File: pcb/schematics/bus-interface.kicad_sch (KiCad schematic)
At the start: 28 parts, among them U3 LCMXO2-1200HC-4TG100I

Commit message: add shield
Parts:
- U: renamed from C31; value 1u -> (none); footprint Capacitor_SMD:C_0805_2012Metric -> (none)
- U: renamed from C24; value 10n -> (none); footprint Capacitor_SMD:C_0402_1005Metric -> (none)
- U: renamed from C22; value 100n -> (none); footprint Capacitor_SMD:C_0603_1608Metric -> (none)
- U: renamed from U3; value LCMXO2-1200HC-4TG100I -> (none); footprint LCMXO2-1200HC-4TG100I:Lattice_Semiconductor-LCMXO2-1200HC-4TG100I-Level_C -> (none)
- U: renamed from C21; value 100n -> (none); footprint Capacitor_SMD:C_0603_1608Metric -> (none)
- U: renamed from C8; value 10n -> (none); footprint Capacitor_SMD:C_0402_1005Metric -> (none)
- U: renamed from C9; value 10n -> (none); footprint Capacitor_SMD:C_0402_1005Metric -> (none)
- U: renamed from C28; value 10n -> (none); footprint Capacitor_SMD:C_0402_1005Metric -> (none)
- U: renamed from C29; value 100n -> (none); footprint Capacitor_SMD:C_0603_1608Metric -> (none)
- U: renamed from C30; value 100n -> (none); footprint Capacitor_SMD:C_0603_1608Metric -> (none)
- U: renamed from C5; value 1u -> (none); footprint Capacitor_SMD:C_0805_2012Metric -> (none)
- U: renamed from C10; value 10n -> (none); footprint Capacitor_SMD:C_0402_1005Metric -> (none)
- U: renamed from C26; value 10n -> (none); footprint Capacitor_SMD:C_0402_1005Metric -> (none)
- U: renamed from C18; value 100n -> (none); footprint Capacitor_SMD:C_0603_1608Metric -> (none)
- U: renamed from C6; value 100n -> (none); footprint Capacitor_SMD:C_0603_1608Metric -> (none)
- U: renamed from C25; value 10n -> (none); footprint Capacitor_SMD:C_0402_1005Metric -> (none)
- U: renamed from C20; value 1u -> (none); footprint Capacitor_SMD:C_0805_2012Metric -> (none)
- U: renamed from C7; value 100n -> (none); footprint Capacitor_SMD:C_0603_1608Metric -> (none)
- U: renamed from C14; value 1u -> (none); footprint Capacitor_SMD:C_0805_2012Metric -> (none)
- U: renamed from C12; value 100n -> (none); footprint Capacitor_SMD:C_0603_1608Metric -> (none)
- U: renamed from C23; value 100n -> (none); footprint Capacitor_SMD:C_0603_1608Metric -> (none)
- U: renamed from C27; value 10n -> (none); footprint Capacitor_SMD:C_0402_1005Metric -> (none)
- U: renamed from C17; value 100n -> (none); footprint Capacitor_SMD:C_0603_1608Metric -> (none)
- U: renamed from C19; value 1u -> (none); footprint Capacitor_SMD:C_0805_2012Metric -> (none)
- U: renamed from C15; value 10n -> (none); footprint Capacitor_SMD:C_0402_1005Metric -> (none)
- U: renamed from C13; value 100n -> (none); footprint Capacitor_SMD:C_0603_1608Metric -> (none)
- U: renamed from C11; value 10n -> (none); footprint Capacitor_SMD:C_0402_1005Metric -> (none)
- U: renamed from C16; value 10n -> (none); footprint Capacitor_SMD:C_0402_1005Metric -> (none)
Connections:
- net +3V3: now also U.91 (PT11C/TCK/TEST_CLK); no longer U.100 (VCC), U.11 (VCCIO3), U.23 (VCCIO3), U.26 (VCCIO2), U.46 (VCCIO2), U.5 (VCCIO3), U.50 (VCC), U.55 (VCCIO1), U.73 (VCCIO1), U.80 (VCCIO0), U.93 (VCCIO0)
- net BUS_CTRL_CONFIG_SN: now also U.76 (PT17D/DONE); no longer U.48 (PB20C/SN)
- net CCK: now also U.95 (PT10C/TDO); no longer U.31 (PB6C/MCLK/CCLK)
- net CONN_0: no longer U.25 (PL10D)
- net CONN_1: now also U.76 (PT17D/DONE); no longer U.24 (PL10C)
- net CONN_10: now also U.87 (PT12B/PCLKC0_1); no longer U.13 (PL5B/PCLKC3_1)
- net CONN_11: now also U.88 (PT12A/PCLKT0_1); no longer U.12 (PL5A/PCLKT3_1)
- net CONN_12: now also U.90 (PT11D/TMS); no longer U.10 (PL4B)
- net CONN_13: now also U.91 (PT11C/TCK/TEST_CLK); no longer U.9 (PL4A)
- net CONN_14: now also U.94 (PT10D/TDI); no longer U.8 (PL3D)
- net CONN_15: now also U.95 (PT10C/TDO); no longer U.7 (PL3C)
- net CONN_16: now also U.96 (PT10B); no longer U.4 (PL3B/PCLKC3_2)
- net CONN_17: now also U.97 (PT10A); no longer U.3 (PL3A/PCLKT3_2)
- net CONN_18: now also U.98 (PT9B); no longer U.2 (PL2D/L_GPLLC_IN)
- net CONN_19: now also U.99 (PT9A); no longer U.1 (PL2C/L_GPLLT_IN)
- net CONN_2: now also U.77 (PT17C/INITN); no longer U.21 (PL9B/PCLKC3_0)
- net CONN_3: now also U.78 (PT16C); no longer U.20 (PL9A/PCLKT3_0)
- net CONN_35: now also U.99 (PT9A); no longer U.75 (PR2A/(DQ0))
- net CONN_36: now also U.98 (PT9B); no longer U.74 (PR2B/(DQ0))
- net CONN_37: now also U.97 (PT10A); no longer U.71 (PR3A/(DQ0))
- net CONN_38: now also U.96 (PT10B); no longer U.70 (PR3B/(DQ0))
- net CONN_39: now also U.95 (PT10C/TDO); no longer U.69 (PR4A/(DQ0))
- net CONN_4: now also U.81 (PT15D/PROGRAMN); no longer U.19 (PL8D)
- net CONN_40: now also U.94 (PT10D/TDI); no longer U.68 (PR4B/(DQ0))
- net CONN_41: now also U.91 (PT11C/TCK/TEST_CLK); no longer U.67 (PR4C/(DQ0))
- net CONN_42: now also U.87 (PT12B/PCLKC0_1); no longer U.64 (PR5B/(DQS0N))
- net CONN_43: now also U.86 (PT12C/SCL/PCLKT0_0); no longer U.63 (PR5C/PCLKT1_0/(DQ0))
- net CONN_44: now also U.85 (PT12D/SDA/PCLKC0_0); no longer U.62 (PR5D/PCLKC1_0/(DQ0))
- net CONN_45: now also U.84 (PT15A); no longer U.61 (PR8A/(DQS1))
- net CONN_46: now also U.82 (PT15C/JTAGENB); no longer U.59 (PR8D/(DQ1))
- net CONN_47: now also U.81 (PT15D/PROGRAMN); no longer U.58 (PR9A/(DQ1))
- net CONN_48: now also U.78 (PT16C); no longer U.57 (PR9B/(DQ1))
- net CONN_49: now also U.77 (PT17C/INITN); no longer U.54 (PR9C/(DQ1))
- net CONN_5: now also U.82 (PT15C/JTAGENB); no longer U.18 (PL8C)
- net CONN_50: now also U.76 (PT17D/DONE); no longer U.53 (PR9D/(DQ1))
- net CONN_51: no longer U.52 (PR10C/(DQ1))
- net CONN_52: no longer U.51 (PR10D/(DQ1))
- net CONN_6: now also U.83 (PT15B); no longer U.17 (PL8B)
- net CONN_7: now also U.84 (PT15A); no longer U.16 (PL8A)
- net CONN_8: now also U.85 (PT12D/SDA/PCLKC0_0); no longer U.15 (PL5D)
- net CONN_9: now also U.86 (PT12C/SCL/PCLKT0_0); no longer U.14 (PL5C)
- net GND: no longer U.22 (GND), U.33 (GND), U.44 (GND), U.56 (GND), U.6 (GND), U.72 (GND), U.79 (GND), U.92 (GND)
- net MISO: now also U.94 (PT10D/TDI); no longer U.32 (PB6D/SO/SPISO)
- net MOSI: no longer U.49 (PB20D/SI/SISPI)

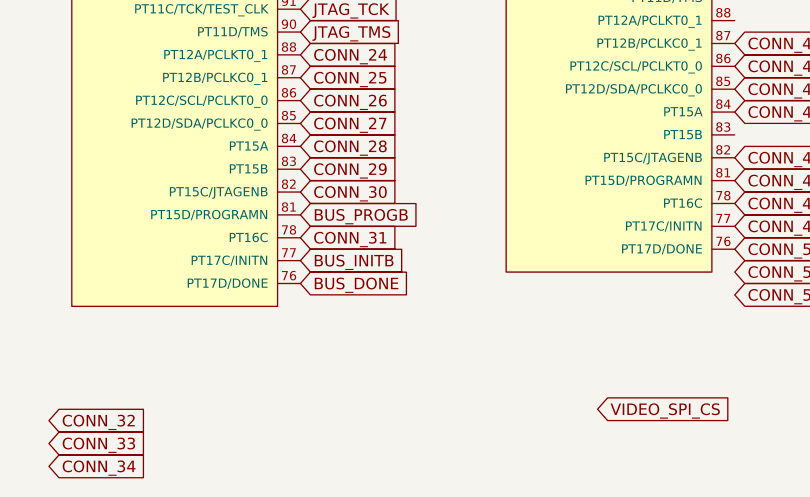
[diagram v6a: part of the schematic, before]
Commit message: add status led in the programming interface schematic
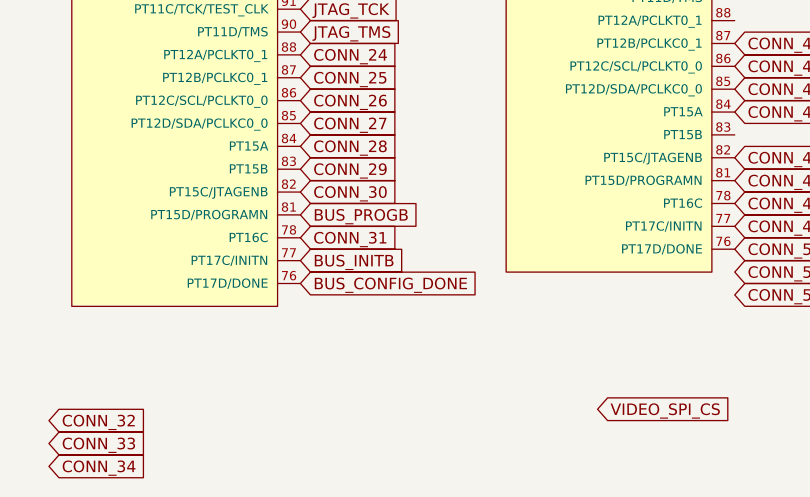
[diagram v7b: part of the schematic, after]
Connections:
- net BUS_DONE renamed BUS_CONFIG_DONE
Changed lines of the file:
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@@
     )
   )
-  (global_label "BUS_DONE" (shape input) (at 121.92 149.86 0)
+  (global_label "BUS_CONFIG_DONE" (shape input) (at 121.92 149.86 0)
     (effects (font (size 1.27 1.27)) (justify left))
     (property "Intersheet References" "${INTERSHEET_REFS}" (id 0) (at 134.2512 149.7806 0)
